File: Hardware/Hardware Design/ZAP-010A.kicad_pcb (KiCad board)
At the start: 2 copper layers, 105 x 58 mm, 79 parts, among them J1 Screw_Terminal_01x04, J2 USB_C_Receptacle_USB2.0_16P, J3 Conn_01x04_Pin, K1 Relay_SPDT, Q1 AO3400A, Q2 AO3400A, SW1 SW_Push, SW2 SW_Push, SW3 SW_Push, SW4 SW_Push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

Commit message: PCB layout and arrangements are done
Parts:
- added TP7: GND, Test Point:TestPoint_Pad_D2.5mm, F.Cu at (123.4, 95.3)
- TP1, TP2, TP3, TP4, TP5, TP6: footprint TestPoint:TestPoint_2Pads_Pitch5.08mm_Drill1.3mm -> Test Point:TestPoint_Pad_D2.5mm
- moved TP2 172.7 mm to (98.5, 65.8)
- moved TP1 172.5 mm to (98.5, 62.1)
- moved D4 161.2 mm to (113.0, 63.6), turned to 90 degrees
- moved Q2 141.5 mm to (104.7, 61.2)
- moved SW2 139.7 mm to (99.1, 75.1), turned to 90 degrees
- moved Q1 135.6 mm to (109.0, 62.0), turned to 90 degrees
- moved U3 129.9 mm to (65.2, 56.9)
- moved C2 125.8 mm to (107.8, 73.7), turned to 90 degrees
- moved FID3 124.5 mm to (152.3, 41.9)
- moved R1 111.4 mm to (130.6, 57.0), turned to 90 degrees
- moved D3 100.1 mm to (123.8, 62.8)
- moved R10 93.9 mm to (118.1, 63.2)
- moved R8 90.9 mm to (105.3, 65.2), turned to 90 degrees
- moved R9 83.6 mm to (108.8, 65.6)
- moved R26 83.2 mm to (100.5, 57.9)
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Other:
- outline, holes or cut-outs redrawn

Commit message: Routing
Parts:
- R1: footprint Resistor_SMD:R_0603_1608Metric -> Resistor_THT:R_Axial_DIN0204_L3.6mm_D1.6mm_P5.08mm_Horizontal
- moved J3 8.50 mm to (57.5, 48.5), turned to 90 degrees
- moved R21 7.40 mm to (60.6, 52.1)
- moved R22 6.70 mm to (67.8, 52.1)
- moved TP4 5.05 mm to (124.2, 95.2)
- moved F1 4.19 mm to (152.3, 47.8), turned to -90 degrees
- moved TP7 3.93 mm to (119.5, 95.2)
- moved R7 2.76 mm to (70.5, 60.3)
- moved R6 2.66 mm to (70.5, 58.5)
- moved R5 2.55 mm to (62.3, 60.7)
- moved C14 2.52 mm to (57.9, 66.0)
- moved J2 2.52 mm to (54.7, 59.0)
- moved D2 2.52 mm to (61.7, 67.7)
- moved U3 2.36 mm to (65.8, 59.2)
- moved R1 2.16 mm to (130.4, 59.1)
- moved SW1 1.71 mm to (60.8, 95.7)
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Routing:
- net +5V: track 0.00 -> 133.6 mm, vias 0 -> 1
- net +3.3V: track 0.00 -> 131.9 mm, vias 0 -> 1
- net SW1/IO11: track 0.00 -> 56.0 mm, vias 0 -> 1
- net NEUTRAL: track 0.00 -> 52.1 mm
- net Net-(PS1-AC/L): track 0.00 -> 51.1 mm
- net SW4/IO14: track 0.00 -> 49.1 mm
- net SCL/IO9: track 0.00 -> 47.0 mm, vias 0 -> 1
- net SDA/IO8: track 0.00 -> 45.8 mm, vias 0 -> 3
- net SL/IO3: track 0.00 -> 42.4 mm
- net CHIP-PU/RST/EN: track 0.00 -> 30.2 mm, vias 0 -> 1
- net SW3/IO13: track 0.00 -> 29.9 mm
- net R-C: track 0.00 -> 23.3 mm
- net SW2/IO12: track 0.00 -> 22.4 mm
- net RELAY/IO2: track 0.00 -> 22.3 mm
- net Net-(J3-Pin_4): track 0.00 -> 21.4 mm
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
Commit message: Routing completed
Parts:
- turned C3 to 180 degrees
- turned C4 to 180 degrees
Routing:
- net EL/IO4: track 14.0 -> 56.7 mm, vias 1 -> 4
- net CHIP-PU/RST/EN: track 30.2 -> 69.5 mm, vias 1 -> 2
- net SW2/IO12: track 22.4 -> 32.0 mm, vias 0 -> 1
- net SW3/IO13: track 29.9 -> 39.4 mm
- net VBUS: track 16.7 -> 22.5 mm
- net Net-(Q2-G): track 0.00 -> 4.78 mm
- net +5V: track 133.6 -> 130.0 mm, vias 1 -> 2
- net Net-(D7-A): track 3.29 -> 6.71 mm
- net +3.3V: track 131.9 -> 134.0 mm
- net SW1/IO11: track 56.0 -> 55.4 mm
- added copper zone on F.Cu, net +3.3V
- added copper zone on F.Cu, net +5V
- added copper zone on B.Cu, net GND
- added copper zone on F.Cu, net GND
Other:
- outline, holes or cut-outs redrawn
- board text added: "NETWORK"
- board text added: "POWER"
- board text added: "STATUS"

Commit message: ERC and DRC done
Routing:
- net +5V: track 130.0 -> 130.4 mm, vias 2 -> 3
- net SDA/IO8: track 45.8 -> 45.9 mm, vias 3 -> 4
- net CHIP-PU/RST/EN: track 69.5 -> 69.6 mm, vias 2 -> 3
- net SCL/IO9: vias 1 -> 2
- net +3.3V: vias 1 -> 0
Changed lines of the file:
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@@
 		(tags "THT terminal block MaiXu MX126-5.0-04P pitch 5mm size 20.5x7.8mm drill 1.3mm pad 2.8mm")
 		(property "Reference" "J1"
-			(at 7.25 -5.12 0)
+			(at -3.5 -5.95 0)
 			(layer "F.SilkS")
 			(effects
@@
 	)
 	(segment
+		(start 100.499998 55.650002)
+		(end 99.3 56.85)
+		(width 0.5)
+		(layer "F.Cu")
+		(net 5)
+	)
+	(segment
 		(start 124.15 77.5525)
 		(end 116.6975 70.1)
@@
 	)
 	(segment
+		(start 100.499998 55.35)
+		(end 100.499998 55.650002)
+		(width 0.5)
+		(layer "F.Cu")
+		(net 5)
+	)
+	(segment
 		(start 103.35 58.25)
 		(end 104.6 58.25)
@@
 	)
 	(via
+		(at 99.3 56.85)
+		(size 0.6)
+		(drill 0.3)
+		(layers "F.Cu" "B.Cu")
+		(net 5)
+	)
+	(via
 		(at 104.6 58.25)
 		(size 0.6)
@@
 	)
 	(segment
+		(start 99.05 56.85)
+		(end 99.3 56.85)
+		(width 0.5)
+		(layer "B.Cu")
+		(net 5)
+	)
+	(segment
 		(start 104.6 64.9)
 		(end 109.85 70.15)
@@
 	)
 	(segment
-		(start 94.15 61.75)
-		(end 100.35 55.55)
+		(start 109.85 70.15)
+		(end 109.9 70.1)
 		(width 0.5)
 		(layer "B.Cu")
@@
 	)
 	(segment
-		(start 109.85 70.15)
-		(end 109.9 70.1)
+		(start 94.15 61.75)
+		(end 99.05 56.85)
 		(width 0.5)
 		(layer "B.Cu")
@@
 		(net 6)
 	)
-	(via
-		(at 64.712499 74.337501)
-		(size 0.6)
-		(drill 0.3)
-		(layers "F.Cu" "B.Cu")
-		(net 6)
-	)
 	(segment
 		(start 79.43 49.82)
@@
 	)
 	(segment
+		(start 73.7 53.15)
+		(end 75.65 53.15)
+		(width 0.3)
+		(layer "F.Cu")
+		(net 7)
+	)
+	(segment
 		(start 65.25 89.2)
 		(end 65.25 95.7)
@@
 	)
 	(via
+		(at 75.65 53.15)
+		(size 0.45)
+		(drill 0.3)
+		(layers "F.Cu" "B.Cu")
+		(net 7)
+	)
+	(via
 		(at 75.05 55.55)
 		(size 0.45)
@@
 	)
 	(segment
+		(start 76.1 53.15)
+		(end 79.45 49.8)
+		(width 0.3)
+		(layer "B.Cu")
+		(net 7)
+	)
+	(segment
 		(start 65.25 89.2)
 		(end 63.85 87.8)
@@
 	)
 	(segment
-		(start 76.15 53.1)
-		(end 73.8 53.1)
-		(width 0.3)
-		(layer "B.Cu")
-		(net 7)
-	)
-	(segment
-		(start 79.45 49.8)
-		(end 76.15 53.1)
+		(start 75.65 53.15)
+		(end 76.1 53.15)
 		(width 0.3)
 		(layer "B.Cu")
@@
 	)
 	(segment
+		(start 62.5 52.95)
+		(end 62.5 53)
+		(width 0.3)
+		(layer "F.Cu")
+		(net 41)
+	)
+	(segment
+		(start 62.5 53)
+		(end 63.25 53.75)
+		(width 0.3)
+		(layer "F.Cu")
+		(net 41)
+	)
+	(segment
 		(start 80.127 67.2)
 		(end 81.655 65.672)
@@
 	)
 	(via
+		(at 63.25 53.75)
+		(size 0.45)
+		(drill 0.3)
+		(layers "F.Cu" "B.Cu")
+		(net 41)
+	)
+	(via
 		(at 79.45 56.5)
 		(size 0.45)
@@
 	)
 	(segment
-		(start 79.45 56.5)
-		(end 78.876 55.926)
+		(start 64.25 54.75)
+		(end 76.95 54.75)
 		(width 0.3)
 		(layer "B.Cu")
@@
 	)
 	(segment
-		(start 78.126 55.926)
-		(end 77 54.8)
+		(start 76.95 54.75)
+		(end 78.126 55.926)
 		(width 0.3)
 		(layer "B.Cu")
@@
 	)
 	(segment
-		(start 78.876 55.926)
-		(end 78.126 55.926)
+		(start 78.126 55.926)
+		(end 78.876 55.926)
 		(width 0.3)
 		(layer "B.Cu")
@@
 	)
 	(segment
-		(start 77 54.8)
-		(end 64.25 54.8)
+		(start 63.25 53.75)
+		(end 64.25 54.75)
 		(width 0.3)
 		(layer "B.Cu")
@@
 	)
 	(segment
-		(start 64.25 54.8)
-		(end 62.45 53)
+		(start 78.876 55.926)
+		(end 79.45 56.5)
 		(width 0.3)
 		(layer "B.Cu")
@@
 	)
 	(segment
+		(start 65.95 52.95)
+		(end 66.75 53.75)
+		(width 0.3)
+		(layer "F.Cu")
+		(net 42)
+	)
+	(segment
 		(start 78.85 62.45)
 		(end 78.9 62.5)
@@
 	)
 	(via
+		(at 66.75 53.75)
+		(size 0.45)
+		(drill 0.3)
+		(layers "F.Cu" "B.Cu")
+		(net 42)
+	)
+	(via
 		(at 78.35 69.15)
 		(size 0.45)
@@
 	)
 	(segment
-		(start 67.05 54.1)
-		(end 66 53.05)
+		(start 78.35 69.15)
+		(end 78.9 68.6)
 		(width 0.3)
 		(layer "B.Cu")
@@
 	)
 	(segment
-		(start 78.35 69.15)
-		(end 78.9 68.6)
+		(start 66.75 53.8)
+		(end 67.05 54.1)
+		(width 0.3)
+		(layer "B.Cu")
+		(net 42)
+	)
+	(segment
+		(start 66.75 53.75)
+		(end 66.75 53.8)
 		(width 0.3)
 		(layer "B.Cu")

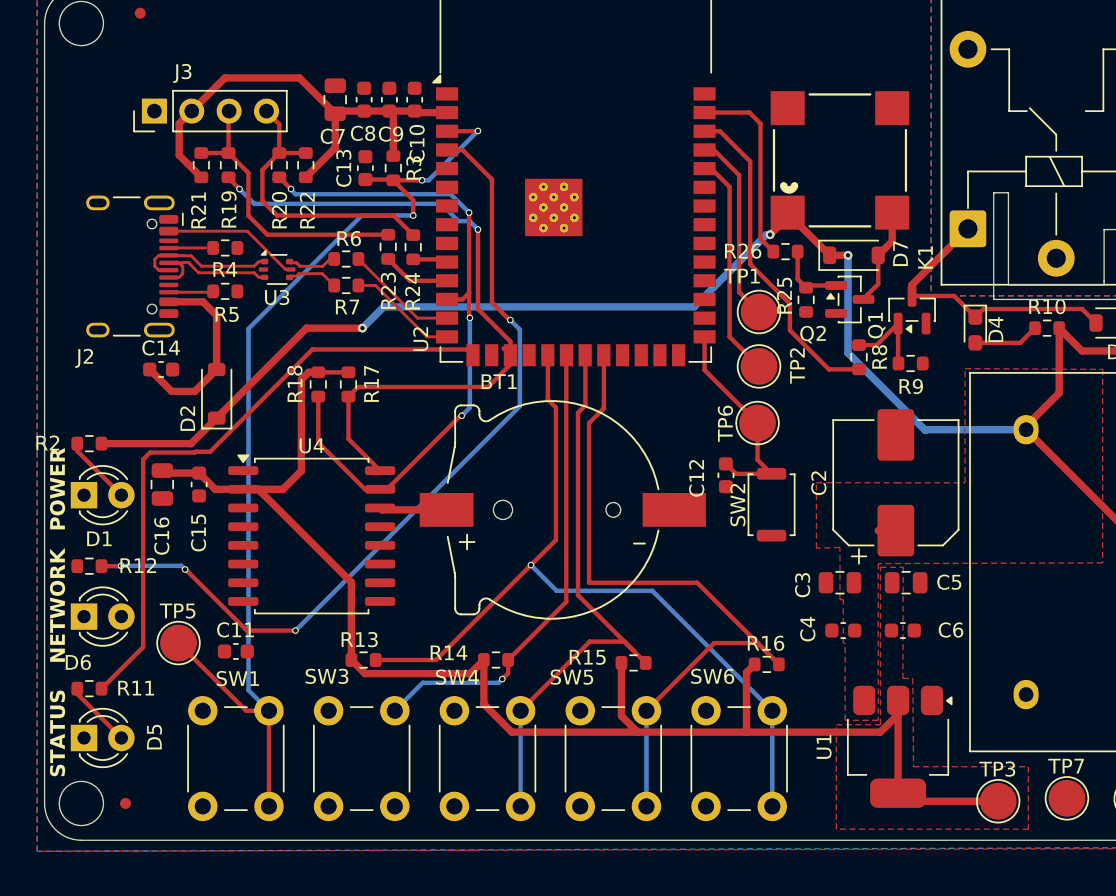
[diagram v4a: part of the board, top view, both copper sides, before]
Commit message: DRC errors cleared
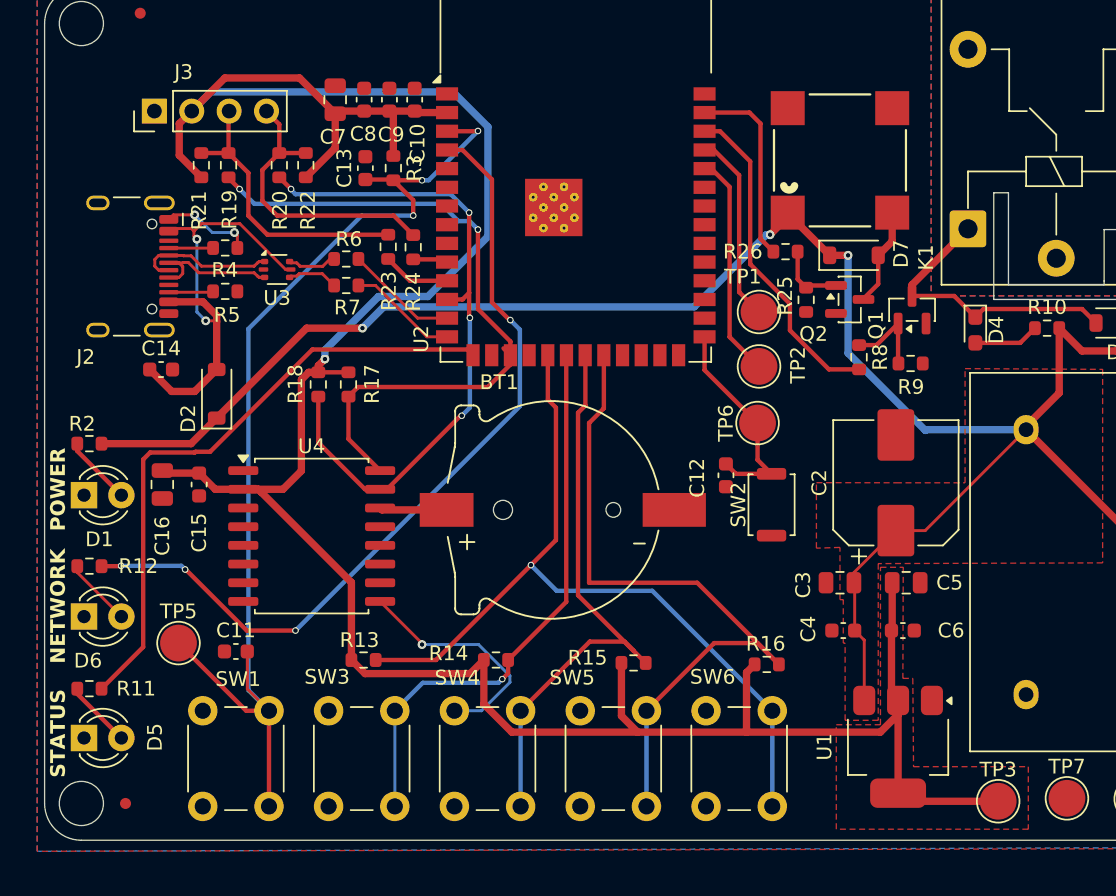
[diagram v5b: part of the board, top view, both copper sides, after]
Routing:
- net +3.3V: track 134.0 -> 187.3 mm, vias 0 -> 1
- net +5V: track 130.4 -> 153.9 mm
- net GND: track 0.00 -> 22.3 mm, vias 0 -> 3
- net VBUS: track 22.5 -> 30.2 mm, vias 0 -> 2
- net SW2/IO12: track 32.0 -> 38.5 mm
- net Net-(D6-A): track 0.00 -> 4.67 mm
- net CHIP-PU/RST/EN: track 69.6 -> 74.2 mm
- net Net-(J2-CC1): track 2.51 -> 3.03 mm
